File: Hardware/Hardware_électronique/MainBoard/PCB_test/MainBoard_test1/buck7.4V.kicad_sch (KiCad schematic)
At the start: 11 parts, among them U2 LT1076CR-PBF

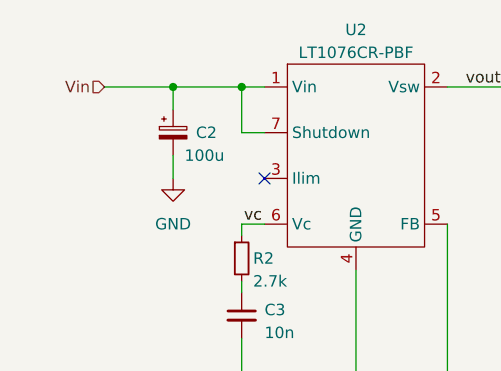
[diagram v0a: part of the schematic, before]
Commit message: Adding motor board
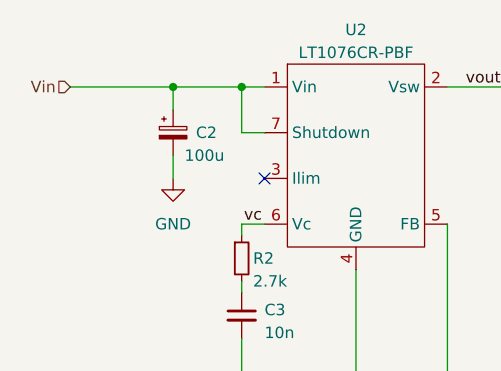
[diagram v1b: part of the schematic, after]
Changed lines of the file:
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@@
+	(wire
+		(pts
+			(xy 72.39 63.5) (xy 83.82 63.5)
+		)
+		(stroke
+			(width 0)
+			(type default)
+		)
+	)
 	(wire
 		(pts
@@
 		(pts
 			(xy 91.44 68.58) (xy 91.44 63.5)
-		)
-		(stroke
-			(width 0)
-			(type default)
-		)
-	)
-	(wire
-		(pts
-			(xy 76.2 63.5) (xy 83.82 63.5)
 		)
 		(stroke
@@
 	(hierarchical_label "Vin"
 		(shape input)
-		(at 76.2 63.5 180)
+		(at 72.39 63.5 180)
 		(fields_autoplaced yes)
 		(effects
@@
 			(justify right)
 		)
-	)
+		(property "14.4V" ""
+			(at 72.39 64.77 0)
+			(effects
+				(font
+					(size 1.27 1.27)
+					(italic yes)
+				)
+				(justify right)
+			)
+		)
+	)
